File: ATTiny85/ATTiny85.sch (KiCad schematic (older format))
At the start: 21 parts, among them J2 Conn_01x05, J3 Conn_01x05, J4 ISP6, SW1 SW_SPST, U1 ATtiny85-20SU

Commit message: Schematic PDF and 3D Renders added
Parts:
- removed PS1: MIC5225YM5_TR, SOT95P280X145-5N, symbol Adjustable_150mA_Regulator:MIC5225YM5_TR
- added U2: AP2127K-3.3, Package_TO_SOT_SMD:SOT-23-5, symbol Regulator_Linear:AP2127K-3.3
- C1: Part (none) -> C29936
- C3, C4: Part (none) -> C95841
- D1, D2: Part (none) -> C232841
- LED1: value SFH460 -> Blue; Part (none) -> C193191
- PWR1: value SFH460 -> Red; Part (none) -> C118330
- R4, R7: Part (none) -> C25585
- R5: value 33k -> 10K; Part (none) -> C99198
- R6, R9: Part (none) -> C325751
- R8: Part (none) -> C114668
- SW1: Part (none) -> C231329
- U1: Part (none) -> 177-2968
- USB1: Part (none) -> C132560
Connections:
- net GND: now also U2.2 (GND)
- net VCC: now also U2.5 (VOUT)
- net at C1.1, C3.1, D1.1 (K)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: now also U2.1 (VIN)
- net at JP1.3 (B): now also U2.3 (EN)
- net 5V renamed VUSB
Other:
- moved on the sheet: C1, C3, C4, D1, D2, J2, J3, J4, JP1, LED1, PWR1, R4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

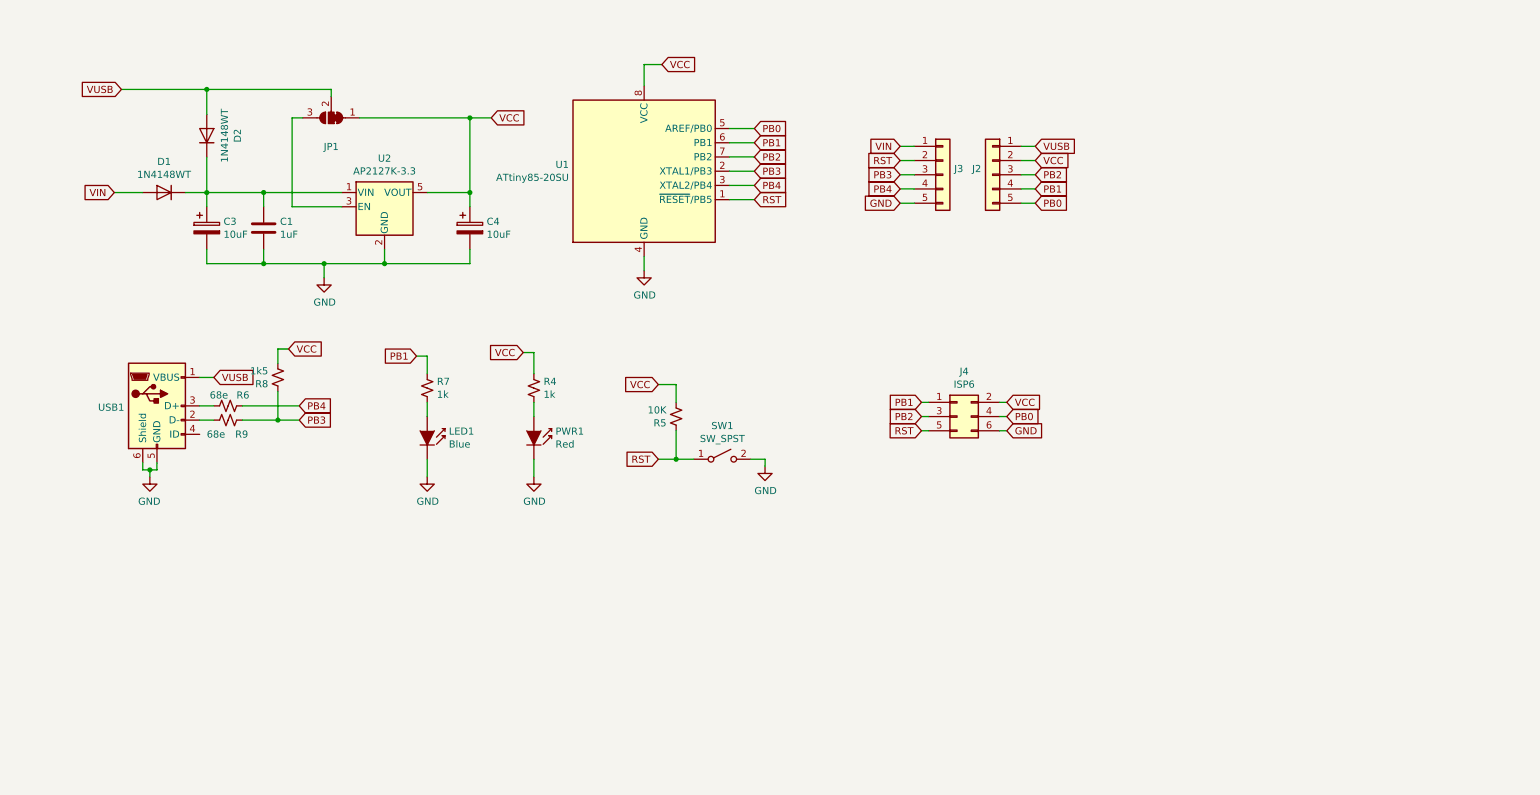
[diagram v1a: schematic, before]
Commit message: ATTiny85 Revision 2
USB-C, SPX3819, QFN Package and Board Size Revision
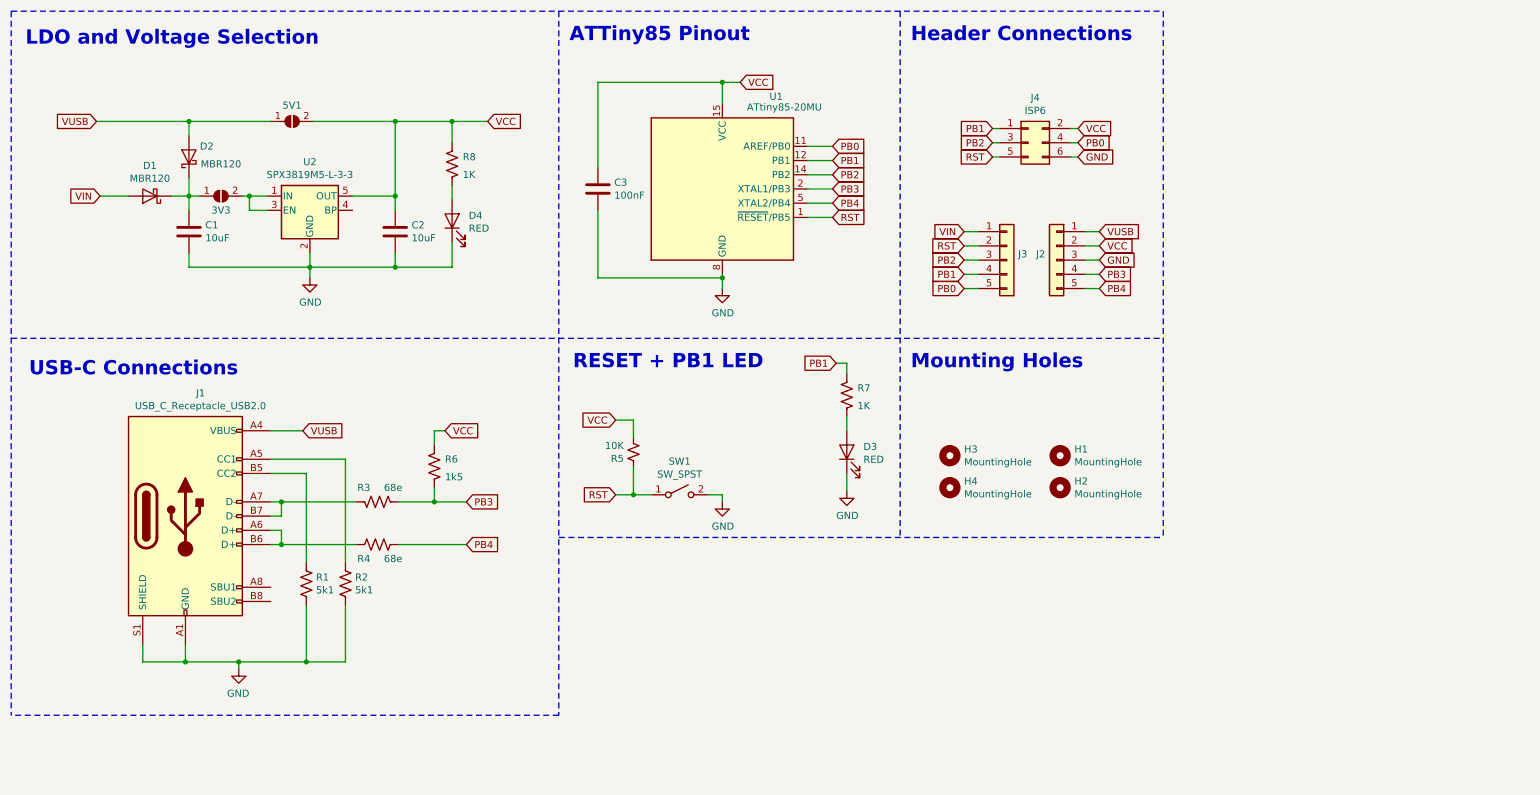
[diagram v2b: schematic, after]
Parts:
- removed C3, C4: 10uF, Capacitor_SMD:C_0805_2012Metric_Pad1.15x1.40mm_HandSolder, symbol Device:CP
- removed D1, D2: 1N4148WT, Diode_SMD:D_SOD-523, symbol Diode:1N4148WT
- removed JP1: SolderJumper_3_Bridged12, Jumper:SolderJumper-3_P1.3mm_Bridged12_RoundedPad1.0x1.5mm, symbol Jumper:SolderJumper_3_Bridged12
- removed LED1: Blue, LED_SMD:LED_0603_1608Metric, symbol LED:SFH460
- removed PWR1: Red, LED_SMD:LED_0603_1608Metric, symbol LED:SFH460
- removed R4, R7: 1k, Resistor_SMD:R_0603_1608Metric, symbol Device:R_Small_US
- removed R6, R9: 68e, Resistor_SMD:R_0603_1608Metric, symbol Device:R_Small_US
- removed R8: 1k5, Resistor_SMD:R_0603_1608Metric, symbol Device:R_Small_US
- removed U1: ATtiny85-20SU, Package_SO:SOIJ-8_5.3x5.3mm_P1.27mm, symbol MCU_Microchip_ATtiny:ATtiny85-20SU
- removed U2: AP2127K-3.3, Package_TO_SOT_SMD:SOT-23-5, symbol Regulator_Linear:AP2127K-3.3
- removed USB1: USB_B_Micro, Connector_USB:USB_Micro-B_Molex_47346-0001, symbol Connector:USB_B_Micro
- added 3V3, 5V1: SolderJumper_2_Open, Jumper:SolderJumper-2_P1.3mm_Open_RoundedPad1.0x1.5mm, symbol Jumper:SolderJumper_2_Open
- added C2: 10uF, Capacitor_SMD:C_0805_2012Metric, symbol Device:C
- added C3: 100nF, Capacitor_SMD:C_0603_1608Metric, symbol Device:C
- added D1, D2: MBR120, Diode_SMD:D_SOD-123, symbol Diode:MBR0520
- added D3, D4: RED, LED_SMD:LED_0603_1608Metric, symbol Device:LED
- added H1, H2, H3, H4: MountingHole, SirBoardLibrary:MountingHole_M2.5_SirBoard, symbol Mechanical:MountingHole
- added J1: USB_C_Receptacle_USB2.0, SirBoardLibrary:USB_C, symbol Connector:USB_C_Receptacle_USB2.0
- added R1, R2: 5k1, Resistor_SMD:R_0603_1608Metric, symbol Device:R_US
- added R3, R4: 68e, Resistor_SMD:R_0603_1608Metric, symbol Device:R_US
- added R6: 1k5, Resistor_SMD:R_0603_1608Metric, symbol Device:R_US
- added R7, R8: 1K, Resistor_SMD:R_0603_1608Metric, symbol Device:R_US
- added U1: ATtiny85-20MU, Package_DFN_QFN:QFN-20-1EP_4x4mm_P0.5mm_EP2.6x2.6mm, symbol MCU_Microchip_ATtiny:ATtiny85-20MU
- added U2: SPX3819M5-L-3-3, Package_TO_SOT_SMD:SOT-23-5, symbol Regulator_Linear:SPX3819M5-L-3-3
- C1: value 1uF -> 10uF; footprint Capacitor_SMD:C_0603_1608Metric -> Capacitor_SMD:C_0805_2012Metric; Part C29936 -> C95841
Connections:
- net GND: now also J2.3 (Pin_3), C2.2, C3.2, D3.1 (K), D4.1 (K), J1.A1 (GND), J1.A12 (GND), J1.B1 (GND), J1.B12 (GND), J1.S1 (SHIELD), R1.2, R2.2, U1.21 (GND), U1.8 (GND), U2.2 (GND); no longer J3.5 (Pin_5)
- net PB0: now also J3.5 (Pin_5), U1.11 (AREF/PB0); no longer J2.5 (Pin_5)
- net PB1: now also J3.4 (Pin_4), R7.2, U1.12 (PB1); no longer J2.4 (Pin_4)
- net PB2: now also J3.3 (Pin_3), U1.14 (PB2); no longer J2.3 (Pin_3)
- net PB3: now also J2.4 (Pin_4), R3.2, R6.1, U1.2 (XTAL1/PB3); no longer J3.3 (Pin_3)
- net PB4: now also J2.5 (Pin_5), R4.2, U1.5 (XTAL2/PB4); no longer J3.4 (Pin_4)
- net RST: now also U1.1 (~RESET~/PB5)
- net VCC: now also 5V1.2 (B), C2.1, C3.1, R6.2, R8.2, U1.15 (VCC), U2.5 (OUT)
- net VIN: now also D1.2 (A)
- net VUSB: now also 5V1.1 (A), D2.2 (A), J1.A4 (VBUS), J1.A9 (VBUS), J1.B4 (VBUS), J1.B9 (VBUS)
- net at C1.1: now also 3V3.1 (A), D1.1 (K), D2.1 (K)
- new net: 3V3.2 (B), U2.1 (IN), U2.3 (EN)
- new net: J1.A5 (CC1), R2.1
- new net: J1.A6 (D+), J1.B6 (D+), R4.1
- new net: J1.A7 (D-), J1.B7 (D-), R3.1
- new net: J1.B5 (CC2), R1.1
- new net: D4.2 (A), R8.1
- new net: D3.2 (A), R7.1
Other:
- note added: "ATTiny85 Pinout"
- note added: "Header Connections"
- note added: "LDO and Voltage Selection"
- note added: "Mounting Holes"
- note added: "RESET + PB1 LED"
- note added: "USB-C Connections"
- moved on the sheet: C1, J2, J3, J4, R5, SW1
